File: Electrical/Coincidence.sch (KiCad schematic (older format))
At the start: 0 parts

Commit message: Added voltage references and test points
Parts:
- added C?: 0.01uF, symbol C
- added C?: 0.1uF, symbol C
- added F?: FERRITE, symbol FERRITE
- added U?: LT1719-S6, symbol LT1719-S6
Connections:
- new net: C?.1, C?.1, F?.2, U?.4
- new net +5VA: F?.1
- new net GND: C?.2, C?.2, U?.2, U?.6
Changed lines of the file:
@@
-EESchema Schematic File Version 2  date 4/17/2013 7:49:12 PM
+EESchema Schematic File Version 2  date 4/18/2013 6:48:03 PM
 LIBS:power
 LIBS:device
@@
 Sheet 2 6
 Title ""
-Date ""
+Date "18 apr 2013"
 Rev ""
 Comp ""
@@
 Comment4 ""
 $EndDescr
+Text HLabel 1700 4100 0    60   Input ~ 0
+ThrsSet
+Wire Wire Line
+	4300 3200 4400 3200
+Wire Wire Line
+	4400 3200 4400 3300
+Connection ~ 3000 2000
+Wire Wire Line
+	3800 2600 3800 2000
+Wire Wire Line
+	3800 2000 2300 2000
+Wire Wire Line
+	2500 2500 2500 2600
+Connection ~ 2500 2000
+Wire Wire Line
+	3000 2000 3000 2100
+Wire Wire Line
+	2500 2000 2500 2100
+Wire Wire Line
+	3000 2600 3000 2500
+Wire Wire Line
+	1600 1900 1600 2000
+Wire Wire Line
+	1600 2000 1700 2000
+Wire Wire Line
+	3800 3500 3800 3400
+$Comp
+L GND #PWR?
+U 1 1 5170724B
+P 4400 3300
+F 0 "#PWR?" H 4400 3300 30  0001 C CNN
+F 1 "GND" H 4400 3230 30  0001 C CNN
+	1    4400 3300
+	1    0    0    -1
+$EndComp
+$Comp
+L GND #PWR?
+U 1 1 51707246
+P 3800 3500
+F 0 "#PWR?" H 3800 3500 30  0001 C CNN
+F 1 "GND" H 3800 3430 30  0001 C CNN
+	1    3800 3500
+	1    0    0    -1
+$EndComp
+$Comp
+L +5VA #PWR?
+U 1 1 517071C6
+P 1600 1900
+F 0 "#PWR?" H 1600 2030 20  0001 C CNN
+F 1 "+5VA" H 1600 2000 30  0000 C CNN
+	1    1600 1900
+	1    0    0    -1
+$EndComp
+$Comp
+L GND #PWR?
+U 1 1 51707183
+P 3000 2600
+F 0 "#PWR?" H 3000 2600 30  0001 C CNN
+F 1 "GND" H 3000 2530 30  0001 C CNN
+	1    3000 2600
+	1    0    0    -1
+$EndComp
+$Comp
+L GND #PWR?
+U 1 1 5170717F
+P 2500 2600
+F 0 "#PWR?" H 2500 2600 30  0001 C CNN
+F 1 "GND" H 2500 2530 30  0001 C CNN
+	1    2500 2600
+	1    0    0    -1
+$EndComp
+$Comp
+L FERRITE F?
+U 1 1 5170716C
+P 2000 2000
+F 0 "F?" H 1900 2100 60  0000 C CNN
+F 1 "FERRITE" H 2100 1900 60  0000 C CNN
+	1    2000 2000
+	1    0    0    -1
+$EndComp
+$Comp
+L C C?
+U 1 1 51707161
+P 2500 2300
+F 0 "C?" H 2550 2400 50  0000 L CNN
+F 1 "0.1uF" H 2550 2200 50  0000 L CNN
+F 4 "16V" H 2500 2300 60  0001 C CNN "Voltage"
+F 5 "X5R" H 2500 2300 60  0001 C CNN "Dielectric"
+	1    2500 2300
+	-1   0    0    -1
+$EndComp
+$Comp
+L C C?
+U 1 1 51707134
+P 3000 2300
+F 0 "C?" H 3050 2400 50  0000 L CNN
+F 1 "0.01uF" H 3050 2200 50  0000 L CNN
+F 4 "16V" H 3000 2300 60  0001 C CNN "Voltage"
+F 5 "X5R" H 3000 2300 60  0001 C CNN "Dielectric"
+	1    3000 2300
+	-1   0    0    -1
+$EndComp
+$Comp
+L LT1719-S6 U?
+U 1 1 51706B71
+P 3900 3000
+F 0 "U?" H 4050 3200 60  0000 C CNN
+F 1 "LT1719-S6" H 3850 3000 60  0000 C CNN
+	1    3900 3000
+	1    0    0    -1
+$EndComp
 $EndSCHEMATC

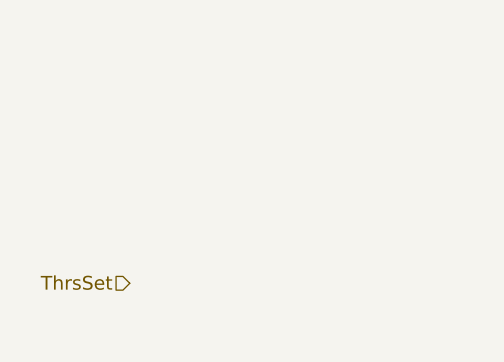
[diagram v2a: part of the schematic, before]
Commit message: Adding schematic annotations to explain functions
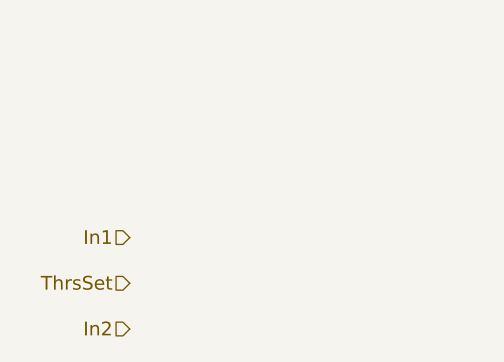
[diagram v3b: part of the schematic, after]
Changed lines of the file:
@@
-EESchema Schematic File Version 2  date 4/18/2013 6:48:03 PM
+EESchema Schematic File Version 2  date 4/18/2013 8:00:54 PM
 LIBS:power
 LIBS:device
@@
 Sheet 2 6
 Title ""
-Date "18 apr 2013"
+Date "19 apr 2013"
 Rev ""
 Comp ""
@@
 Comment4 ""
 $EndDescr
+Text HLabel 1700 4300 0    60   Input ~ 0
+In2
+Text HLabel 1700 3900 0    60   Input ~ 0
+In1
 Text HLabel 1700 4100 0    60   Input ~ 0
 ThrsSet

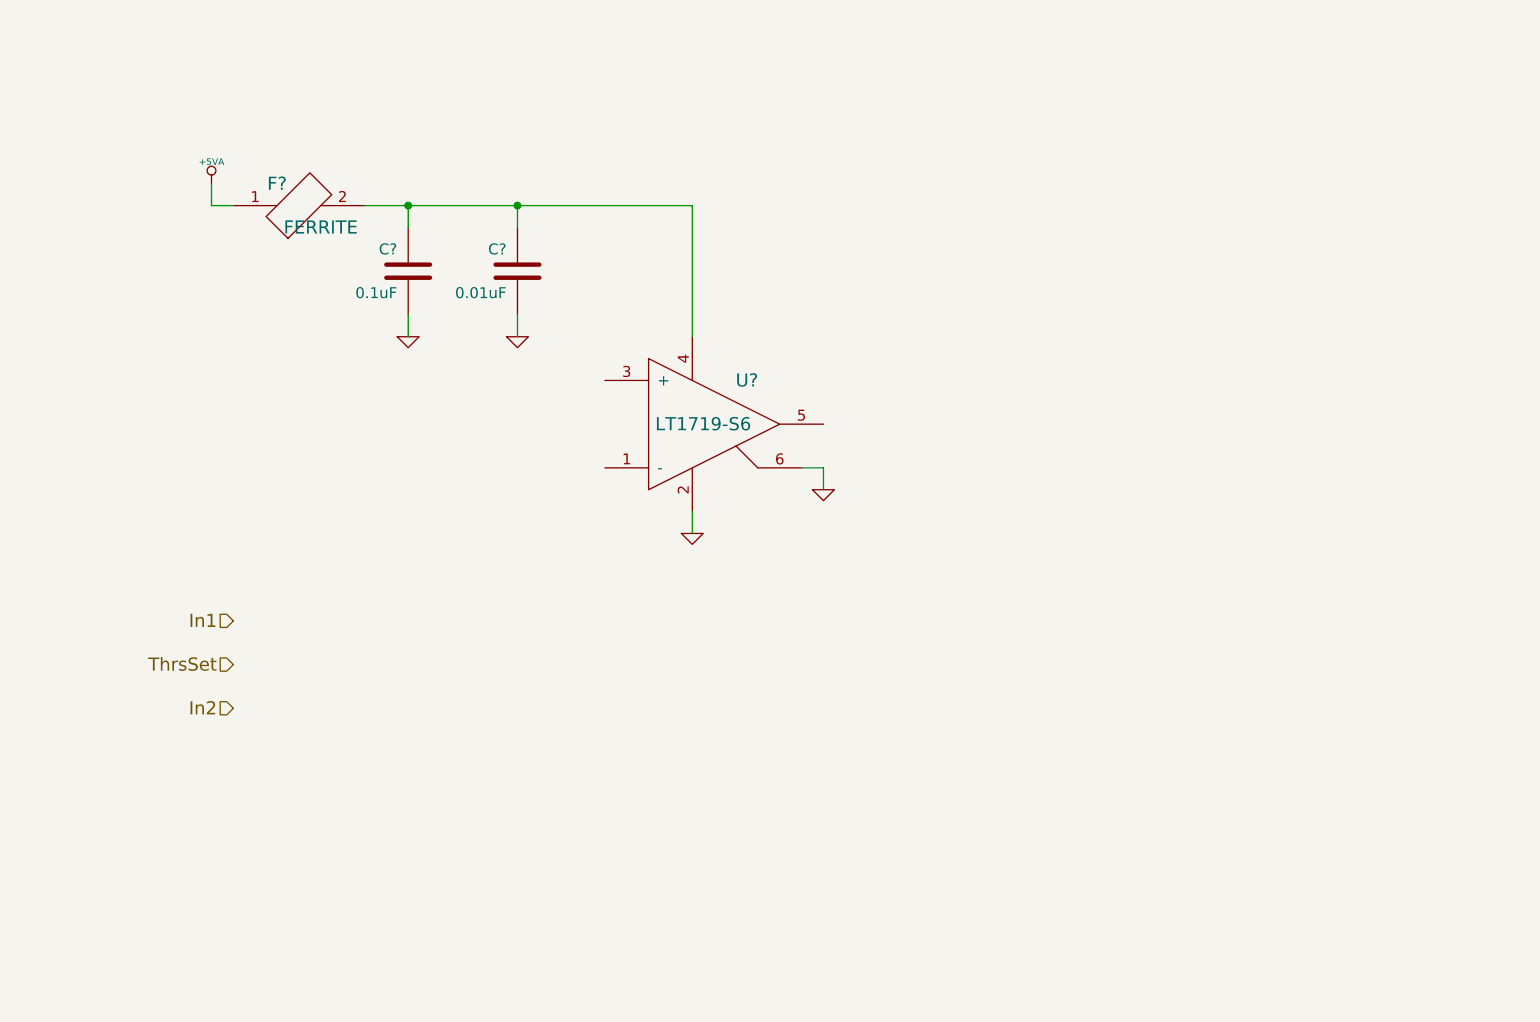
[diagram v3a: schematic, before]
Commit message: Added coincidence circuit to schematic
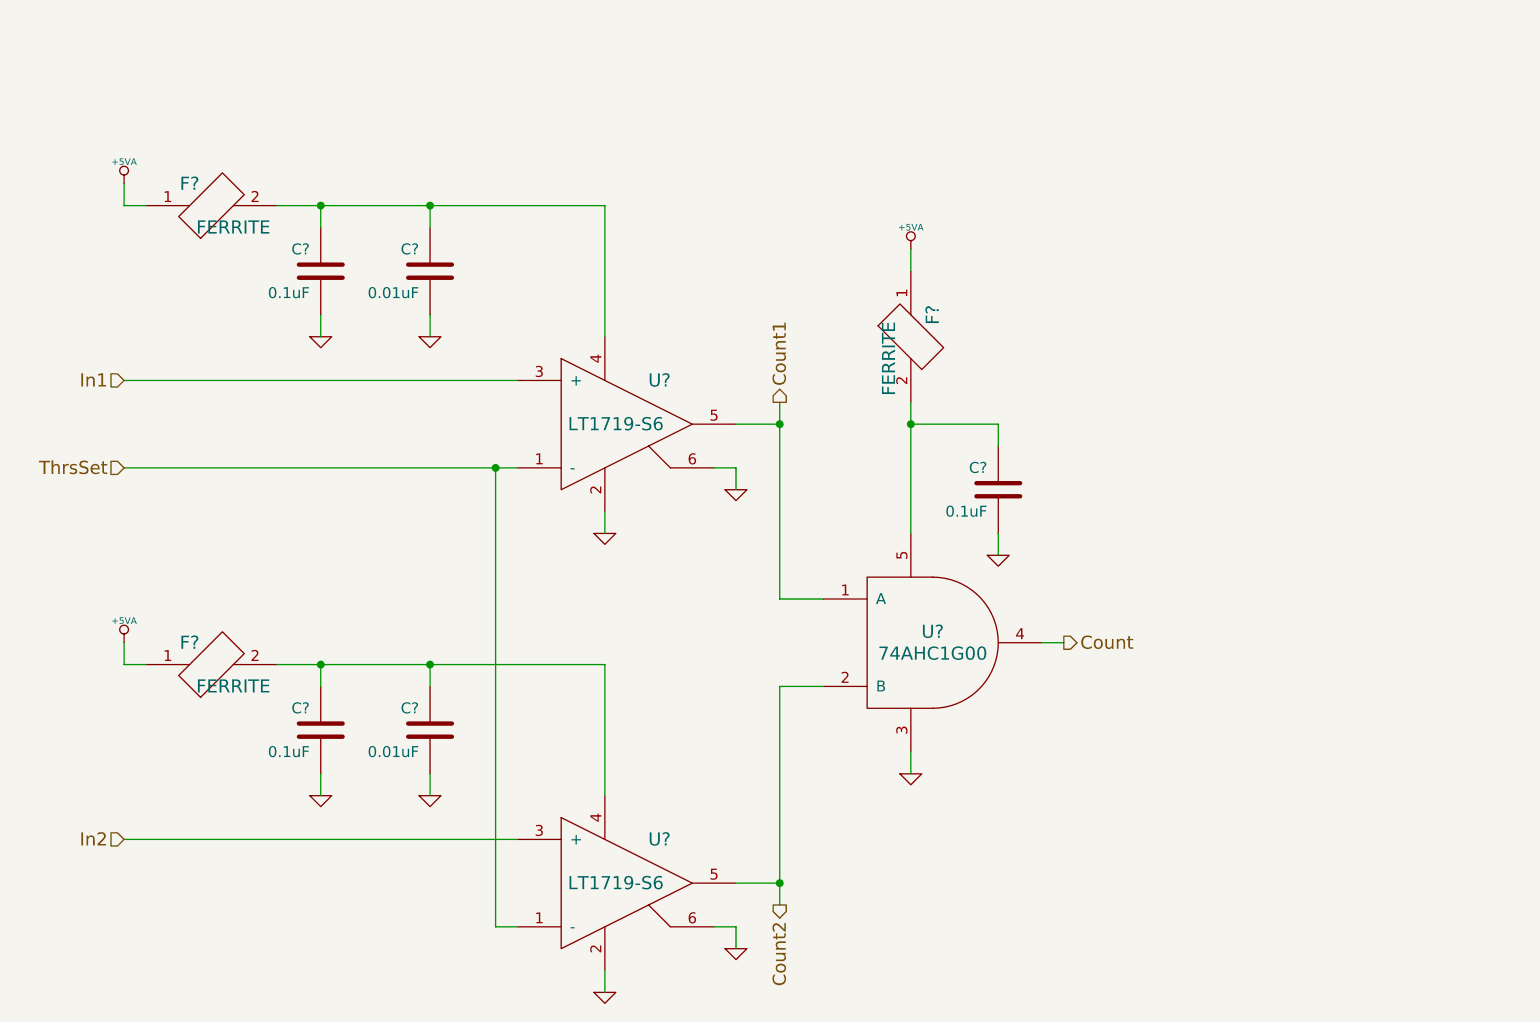
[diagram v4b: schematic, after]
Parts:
- added C? (x2): 0.1uF, symbol C
- added C?: 0.01uF, symbol C
- added F? (x2): FERRITE, symbol FERRITE
- added U?: LT1719-S6, symbol LT1719-S6
- added U?: 74AHC1G00, symbol 74AHC1G00
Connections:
- net +5VA: now also F?.1, F?.1
- net GND: now also C?.2, C?.2, C?.2, U?.2, U?.3, U?.6
- net In1: now also U?.3 (+)
- net In2: now also U?.3 (+)
- net ThrsSet: now also U?.1 (-), U?.1 (-)
- net Count1: now reaches U?.5
- net Count1: now also U?.1 (A)
- new net: C?.1, C?.1, F?.2, U?.4
- new net: C?.1, F?.2, U?.5
- new net Count: U?.4
- new net Count2: U?.2 (B), U?.5
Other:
- moved on the sheet: C?, F?, U?

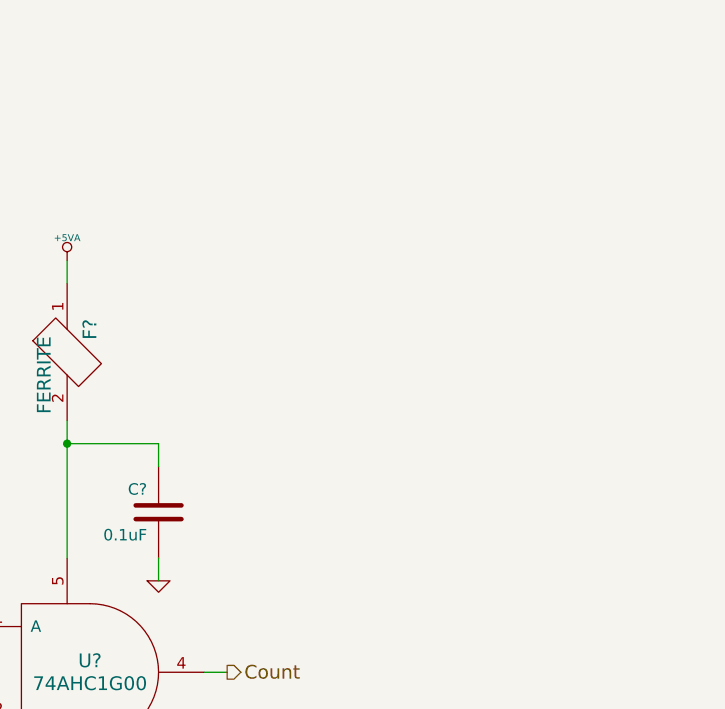
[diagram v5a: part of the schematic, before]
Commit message: Added sensors/data logger with ChipKit Max
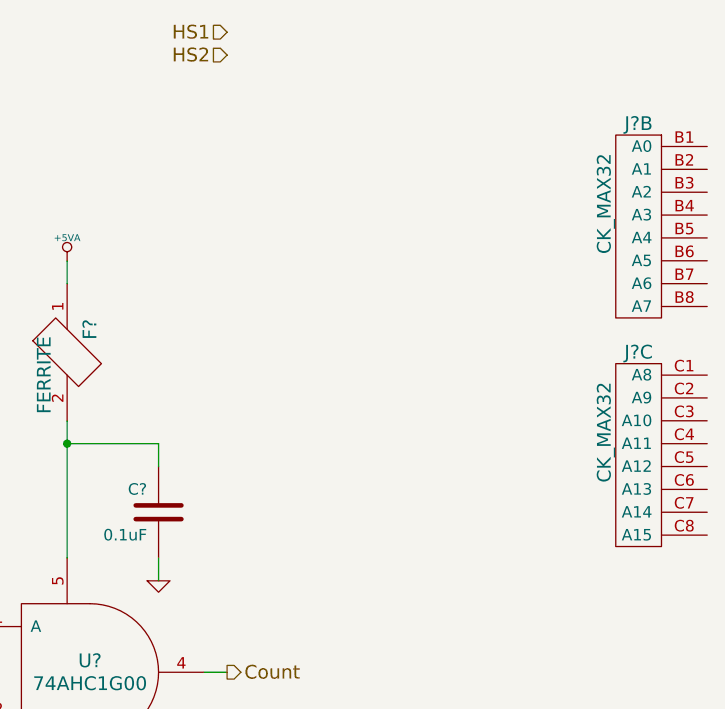
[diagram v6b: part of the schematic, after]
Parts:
- added J? (x2): CK_MAX32, symbol CK_MAX32
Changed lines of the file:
@@
-EESchema Schematic File Version 2  date 4/19/2013 7:14:36 PM
+EESchema Schematic File Version 2  date 5/4/2013 6:32:29 PM
 LIBS:power
 LIBS:device
@@
 $Descr A4 11700 8267
 encoding utf-8
-Sheet 2 6
+Sheet 5 7
 Title ""
-Date "20 apr 2013"
+Date "4 may 2013"
 Rev ""
 Comp ""
@@
 Comment4 ""
 $EndDescr
+Text HLabel 5500 1300 0    60   Input ~ 0
+HS2
+Text HLabel 5500 1200 0    60   Input ~ 0
+HS1
+$Comp
+L CK_MAX32 J?
+U 3 1 51858A0A
+P 7300 2700
+F 0 "J?" H 7300 2800 60  0000 C CNN
+F 1 "CK_MAX32" V 7150 2450 60  0000 C CNN
+	3    7300 2700
+	1    0    0    -1
+$EndComp
+$Comp
+L CK_MAX32 J?
+U 2 1 518589FE
+P 7300 1700
+F 0 "J?" H 7300 1800 60  0000 C CNN
+F 1 "CK_MAX32" V 7150 1450 60  0000 C CNN
+	2    7300 1700
+	1    0    0    -1
+$EndComp
 Wire Wire Line
 	5500 4000 5400 4000

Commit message: Annotated schematic
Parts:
- gave numbers to parts that had none: 12
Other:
- moved on the sheet: J2B, J2C
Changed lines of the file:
@@
-EESchema Schematic File Version 2  date 5/4/2013 6:32:29 PM
+EESchema Schematic File Version 2  date 5/5/2013 3:54:39 PM
 LIBS:power
 LIBS:device
@@
 encoding utf-8
 Sheet 5 7
-Title ""
-Date "4 may 2013"
-Rev ""
-Comp ""
-Comment1 ""
-Comment2 ""
+Title "Cosmic Ray Detector"
+Date "5 may 2013"
+Rev "1A"
+Comp "Ethan Harstad"
+Comment1 "https://github.com/ethanharstad/SiPMCosmicRay"
+Comment2 "CC-BY-SA 3.0 License"
 Comment3 ""
 Comment4 ""
@@
 HS1
 $Comp
-L CK_MAX32 J?
+L CK_MAX32 J2
 U 3 1 51858A0A
-P 7300 2700
-F 0 "J?" H 7300 2800 60  0000 C CNN
-F 1 "CK_MAX32" V 7150 2450 60  0000 C CNN
-	3    7300 2700
-	1    0    0    -1
-$EndComp
-$Comp
-L CK_MAX32 J?
+P 7200 2700
+F 0 "J2" H 7200 2800 60  0000 C CNN
+F 1 "CK_MAX32" V 7050 2450 60  0000 C CNN
+	3    7200 2700
+	1    0    0    -1
+$EndComp
+$Comp
+L CK_MAX32 J2
 U 2 1 518589FE
-P 7300 1700
-F 0 "J?" H 7300 1800 60  0000 C CNN
-F 1 "CK_MAX32" V 7150 1450 60  0000 C CNN
-	2    7300 1700
+P 7200 1700
+F 0 "J2" H 7200 1800 60  0000 C CNN
+F 1 "CK_MAX32" V 7050 1450 60  0000 C CNN
+	2    7200 1700
 	1    0    0    -1
 $EndComp
@@
 Count1
 $Comp
-L FERRITE F?
+L FERRITE FB7
 U 1 1 5170AC01
 P 4800 2600
-F 0 "F?" H 4700 2700 60  0000 C CNN
+F 0 "FB7" H 4700 2700 60  0000 C CNN
 F 1 "FERRITE" H 4900 2500 60  0000 C CNN
 	1    4800 2600
@@
 $EndComp
 $Comp
-L GND #PWR?
+L GND #PWR77
 U 1 1 5170AB91
 P 4800 4600
-F 0 "#PWR?" H 4800 4600 30  0001 C CNN
+F 0 "#PWR77" H 4800 4600 30  0001 C CNN
 F 1 "GND" H 4800 4530 30  0001 C CNN
 	1    4800 4600
@@
 $EndComp
 $Comp
-L +5VA #PWR?
+L +5VA #PWR76
 U 1 1 5170AB82
 P 4800 2200
-F 0 "#PWR?" H 4800 2330 20  0001 C CNN
+F 0 "#PWR76" H 4800 2330 20  0001 C CNN
 F 1 "+5VA" H 4800 2300 30  0000 C CNN
 	1    4800 2200
@@
 $EndComp
 $Comp
-L GND #PWR?
+L GND #PWR78
 U 1 1 5170AB77
 P 5200 3600
-F 0 "#PWR?" H 5200 3600 30  0001 C CNN
+F 0 "#PWR78" H 5200 3600 30  0001 C CNN
 F 1 "GND" H 5200 3530 30  0001 C CNN
 	1    5200 3600
@@
 $EndComp
 $Comp
-L C C?
+L C C33
 U 1 1 5170AB68
 P 5200 3300
-F 0 "C?" H 5250 3400 50  0000 L CNN
+F 0 "C33" H 5250 3400 50  0000 L CNN
 F 1 "0.1uF" H 5250 3200 50  0000 L CNN
 F 4 "16V" H 5200 3300 60  0001 C CNN "Voltage"
@@
 $EndComp
 $Comp
-L 74AHC1G00 U?
+L 74AHC1G00 U11
 U 1 1 5170AB2D
 P 4900 4000
-F 0 "U?" H 4900 4050 60  0000 C CNN
+F 0 "U11" H 4900 4050 60  0000 C CNN
 F 1 "74AHC1G00" H 4900 3950 60  0000 C CNN
 	1    4900 4000
@@
 $EndComp
 $Comp
-L LT1719-S6 U?
+L LT1719-S6 U10
 U 1 1 5170A73B
 P 3500 5100
-F 0 "U?" H 3650 5300 60  0000 C CNN
+F 0 "U10" H 3650 5300 60  0000 C CNN
 F 1 "LT1719-S6" H 3450 5100 60  0000 C CNN
 	1    3500 5100
@@
 $EndComp
 $Comp
-L C C?
+L C C32
 U 1 1 5170A73A
 P 2600 4400
-F 0 "C?" H 2650 4500 50  0000 L CNN
+F 0 "C32" H 2650 4500 50  0000 L CNN
 F 1 "0.01uF" H 2650 4300 50  0000 L CNN
 F 4 "16V" H 2600 4400 60  0001 C CNN "Voltage"
@@
 $EndComp
 $Comp
-L C C?
+L C C30
 U 1 1 5170A739
 P 2100 4400
-F 0 "C?" H 2150 4500 50  0000 L CNN
+F 0 "C30" H 2150 4500 50  0000 L CNN
 F 1 "0.1uF" H 2150 4300 50  0000 L CNN
 F 4 "16V" H 2100 4400 60  0001 C CNN "Voltage"
@@
 $EndComp
 $Comp
-L FERRITE F?
+L FERRITE FB6
 U 1 1 5170A738
 P 1600 4100
-F 0 "F?" H 1500 4200 60  0000 C CNN
+F 0 "FB6" H 1500 4200 60  0000 C CNN
 F 1 "FERRITE" H 1700 4000 60  0000 C CNN
 	1    1600 4100
@@
 $EndComp
 $Comp
-L GND #PWR?
+L GND #PWR69
 U 1 1 5170A737
 P 2100 4700
-F 0 "#PWR?" H 2100 4700 30  0001 C CNN
+F 0 "#PWR69" H 2100 4700 30  0001 C CNN
 F 1 "GND" H 2100 4630 30  0001 C CNN
 	1    2100 4700
@@
 $EndComp
 $Comp
-L GND #PWR?
+L GND #PWR71
 U 1 1 5170A736
 P 2600 4700
-F 0 "#PWR?" H 2600 4700 30  0001 C CNN
+F 0 "#PWR71" H 2600 4700 30  0001 C CNN
 F 1 "GND" H 2600 4630 30  0001 C CNN
 	1    2600 4700
@@
 $EndComp
 $Comp
-L +5VA #PWR?
+L +5VA #PWR67
 U 1 1 5170A735
 P 1200 4000
-F 0 "#PWR?" H 1200 4130 20  0001 C CNN
+F 0 "#PWR67" H 1200 4130 20  0001 C CNN
 F 1 "+5VA" H 1200 4100 30  0000 C CNN
 	1    1200 4000
@@
 $EndComp
 $Comp
-L GND #PWR?
+L GND #PWR73
 U 1 1 5170A734
 P 3400 5600
-F 0 "#PWR?" H 3400 5600 30  0001 C CNN
+F 0 "#PWR73" H 3400 5600 30  0001 C CNN
 F 1 "GND" H 3400 5530 30  0001 C CNN
 	1    3400 5600
@@
 $EndComp
 $Comp
-L GND #PWR?
+L GND #PWR75
 U 1 1 5170A733
 P 4000 5400
-F 0 "#PWR?" H 4000 5400 30  0001 C CNN
+F 0 "#PWR75" H 4000 5400 30  0001 C CNN
 F 1 "GND" H 4000 5330 30  0001 C CNN
 	1    4000 5400
@@
 ThrsSet
 $Comp
-L GND #PWR?
+L GND #PWR74
 U 1 1 5170724B
 P 4000 3300
-F 0 "#PWR?" H 4000 3300 30  0001 C CNN
+F 0 "#PWR74" H 4000 3300 30  0001 C CNN
 F 1 "GND" H 4000 3230 30  0001 C CNN
 	1    4000 3300
@@
 $EndComp
 $Comp
-L GND #PWR?
+L GND #PWR72
 U 1 1 51707246
 P 3400 3500
-F 0 "#PWR?" H 3400 3500 30  0001 C CNN
+F 0 "#PWR72" H 3400 3500 30  0001 C CNN
 F 1 "GND" H 3400 3430 30  0001 C CNN
 	1    3400 3500
@@
 $EndComp
 $Comp
-L +5VA #PWR?
+L +5VA #PWR66
 U 1 1 517071C6
 P 1200 1900
-F 0 "#PWR?" H 1200 2030 20  0001 C CNN
+F 0 "#PWR66" H 1200 2030 20  0001 C CNN
 F 1 "+5VA" H 1200 2000 30  0000 C CNN
 	1    1200 1900
@@
 $EndComp
 $Comp
-L GND #PWR?
+L GND #PWR70
 U 1 1 51707183
 P 2600 2600
-F 0 "#PWR?" H 2600 2600 30  0001 C CNN
+F 0 "#PWR70" H 2600 2600 30  0001 C CNN
 F 1 "GND" H 2600 2530 30  0001 C CNN
 	1    2600 2600
@@
 $EndComp
 $Comp
-L GND #PWR?
+L GND #PWR68
 U 1 1 5170717F
 P 2100 2600
-F 0 "#PWR?" H 2100 2600 30  0001 C CNN
+F 0 "#PWR68" H 2100 2600 30  0001 C CNN
 F 1 "GND" H 2100 2530 30  0001 C CNN
 	1    2100 2600
@@
 $EndComp
 $Comp
-L FERRITE F?
+L FERRITE FB5
 U 1 1 5170716C
 P 1600 2000
-F 0 "F?" H 1500 2100 60  0000 C CNN
+F 0 "FB5" H 1500 2100 60  0000 C CNN
 F 1 "FERRITE" H 1700 1900 60  0000 C CNN
 	1    1600 2000
@@
 $EndComp
 $Comp
-L C C?
+L C C29
 U 1 1 51707161
 P 2100 2300
-F 0 "C?" H 2150 2400 50  0000 L CNN
+F 0 "C29" H 2150 2400 50  0000 L CNN
 F 1 "0.1uF" H 2150 2200 50  0000 L CNN
 F 4 "16V" H 2100 2300 60  0001 C CNN "Voltage"
@@
 $EndComp
 $Comp
-L C C?
+L C C31
 U 1 1 51707134
 P 2600 2300
-F 0 "C?" H 2650 2400 50  0000 L CNN
+F 0 "C31" H 2650 2400 50  0000 L CNN
 F 1 "0.01uF" H 2650 2200 50  0000 L CNN
 F 4 "16V" H 2600 2300 60  0001 C CNN "Voltage"
@@
 $EndComp
 $Comp
-L LT1719-S6 U?
+L LT1719-S6 U9
 U 1 1 51706B71
 P 3500 3000
-F 0 "U?" H 3650 3200 60  0000 C CNN
+F 0 "U9" H 3650 3200 60  0000 C CNN
 F 1 "LT1719-S6" H 3450 3000 60  0000 C CNN
 	1    3500 3000
